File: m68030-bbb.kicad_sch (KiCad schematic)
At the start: 6 parts, among them U1 MC68030, U2 XC95108TQ100, U3 IS61C25616AL, U4 M29F400F, U5 IS61C25616AL, U6 M29F400F

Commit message: Add MPCC and PIT, move things around.  Still need to decide on CPLD to use.
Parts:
- removed U2: XC95108TQ100, Package_QFP:TQFP-100_14x14mm_P0.5mm, symbol CPLD_Xilinx:XC95108PQ100
- removed U3, U5: IS61C25616AL, Package_SO:TSOP-II-44_10.16x18.41mm_P0.8mm, symbol sbc-parts:IS61C25616AL
- removed U4, U6: M29F400F, Package_SO:TSOP-I-48_18.4x12mm_P0.5mm, symbol Memory_Flash:28F400
- added U10, U11, U8, U9: M29F160F, Package_SO:TSOP-I-48_18.4x12mm_P0.5mm, symbol sbc-parts:M29F160F
- added U2: R68561, Package_DIP:DIP-48_W15.24mm_Socket_LongPads, symbol retro-parts:R68561
- added U3: 68230, Package_DIP:DIP-48_W15.24mm_Socket_LongPads, symbol Interface:68230
- added U4, U5, U6, U7: CY62167GN-45ZXI, Package_SO:TSOP-I-48_18.4x12mm_P0.5mm, symbol sbc-parts:CY62167GN-45ZXI
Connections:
- net ~{BR}: now reaches U1.A1 (~{BR})
- net A17: now reaches U1.A10 (A17)
- net A17: now also U10.2 (A14), U11.2 (A14), U4.1 (A15), U5.1 (A15), U6.1 (A15), U7.1 (A15), U8.2 (A14), U9.2 (A14)
- net A15: now reaches U1.A11 (A15)
- net A15: now also U10.4 (A12), U11.4 (A12), U4.3 (A13), U5.3 (A13), U6.3 (A13), U7.3 (A13), U8.4 (A12), U9.4 (A12)
- net A13: now reaches U1.A12 (A13)
- net A13: now also U10.6 (A10), U11.6 (A10), U4.5 (A11), U5.5 (A11), U6.5 (A11), U7.5 (A11), U8.6 (A10), U9.6 (A10)
- net A10: now reaches U1.A13 (A10)
- net A10: now also U10.18 (A7), U11.18 (A7), U4.8 (A8), U5.8 (A8), U6.8 (A8), U7.8 (A8), U8.18 (A7), U9.18 (A7)
- net A0: now reaches U1.A2 (A0)
- net A30: now reaches U1.A3 (A30)
- net A28: now reaches U1.A4 (A28)
- net A26: now reaches U1.A5 (A26)
- net A24: now reaches U1.A6 (A24)
- net A23: now reaches U1.A7 (A23)
- net A21: now reaches U1.A8 (A21)
- net A21: now also U10.16 (A18), U11.16 (A18), U4.9 (A19), U5.9 (A19), U6.9 (A19), U7.9 (A19), U8.16 (A18), U9.16 (A18)
- net A19: now reaches U1.A9 (A19)
- net A19: now also U10.48 (A16), U11.48 (A16), U4.17 (A17), U5.17 (A17), U6.17 (A17), U7.17 (A17), U8.48 (A16), U9.48 (A16)
- net ~{RMC}: now reaches U1.B1 (~{RMC})
- net A14: now reaches U1.B10 (A14)
- net A14: now also U10.5 (A11), U11.5 (A11), U4.4 (A12), U5.4 (A12), U6.4 (A12), U7.4 (A12), U8.5 (A11), U9.5 (A11)
- net A12: now reaches U1.B11 (A12)
- net A12: now also U10.7 (A9), U11.7 (A9), U4.6 (A10), U5.6 (A10), U6.6 (A10), U7.6 (A10), U8.7 (A9), U9.7 (A9)
- net A8: now reaches U1.B12 (A8)
- net A8: now also U10.20 (A5), U11.20 (A5), U4.19 (A6), U5.19 (A6), U6.19 (A6), U7.19 (A6), U8.20 (A5), U9.20 (A5)
- net A7: now reaches U1.B13 (A7)
- net A7: now also U10.21 (A4), U11.21 (A4), U4.20 (A5), U5.20 (A5), U6.20 (A5), U7.20 (A5), U8.21 (A4), U9.21 (A4)
- net ~{BG}: now reaches U1.B2 (~{BG})
- net A31: now reaches U1.B3 (A31)
- net A29: now reaches U1.B4 (A29)
- net A27: now reaches U1.B5 (A27)
- net A25: now reaches U1.B6 (A25)
- net A22: now reaches U1.B7 (A22)
- net A22: now also U10.9 (A19), U11.9 (A19), U4.45 (DQ15/A20), U5.45 (DQ15/A20), U6.45 (DQ15/A20), U7.45 (DQ15/A20), U8.9 (A19), U9.9 (A19)
- net A20: now reaches U1.B8 (A20)
- net A20: now also U10.17 (A17), U11.17 (A17), U4.16 (A18), U5.16 (A18), U6.16 (A18), U7.16 (A18), U8.17 (A17), U9.17 (A17)
- net A16: now reaches U1.B9 (A16)
- net A16: now also U10.3 (A13), U11.3 (A13), U4.2 (A14), U5.2 (A14), U6.2 (A14), U7.2 (A14), U8.3 (A13), U9.3 (A13)
- net FC1: now reaches U1.C1 (FC1)
- net A11: now reaches U1.C10 (A11)
- net A11: now also U10.8 (A8), U11.8 (A8), U4.7 (A9), U5.7 (A9), U6.7 (A9), U7.7 (A9), U8.8 (A8), U9.8 (A8)
- net A9: now reaches U1.C11 (A9)
- net A9: now also U10.19 (A6), U11.19 (A6), U4.18 (A7), U5.18 (A7), U6.18 (A7), U7.18 (A7), U8.19 (A6), U9.19 (A6)
- net A5: now reaches U1.C12 (A5)
- net A5: now also U10.23 (A2), U11.23 (A2), U4.22 (A3), U5.22 (A3), U6.22 (A3), U7.22 (A3), U8.23 (A2), U9.23 (A2)
- net A4: now reaches U1.C13 (A4)
- net A4: now also U10.24 (A1), U11.24 (A1), U4.23 (A2), U5.23 (A2), U6.23 (A2), U7.23 (A2), U8.24 (A1), U9.24 (A1)
- net ~{BGACK}: now reaches U1.C3 (~{BGACK})
- net A1: now reaches U1.C4 (A1)
- net GND: now reaches U1.C5 (GND)
- net GND: now also U1.C7 (GND), U1.C9 (GND), U1.E11 (GND), U1.E3 (GND), U1.F3 (GND), U1.G11 (GND), U1.G3 (GND), U1.J11 (GND), U1.J3 (GND), U1.L5 (GND), U1.L7 (GND), U1.L8 (GND), U1.L9 (GND), U4.27 (VSS), U4.46 (VSS), U4.47 (~{BYTE}), U5.27 (VSS), U5.46 (VSS), U5.47 (~{BYTE}), U6.27 (VSS), U6.46 (VSS), U6.47 (~{BYTE}), U7.27 (VSS), U7.46 (VSS), U7.47 (~{BYTE})
- net +5V: now reaches U1.C6 (VCC)
- net +5V: now also U1.D10 (VCC), U1.D4 (VCC), U1.F11 (VCC), U1.F2 (VCC), U1.H11 (VCC), U1.H3 (VCC), U1.K10 (VCC), U1.K4 (VCC), U1.L6 (VCC)
- net A18: now reaches U1.C8 (A18)
- net A18: now also U10.1 (A15), U11.1 (A15), U4.48 (A16), U5.48 (A16), U6.48 (A16), U7.48 (A16), U8.1 (A15), U9.1 (A15)
- net FC2: now reaches U1.D1 (FC2)
- net A6: now reaches U1.D11 (A6)
- net A6: now also U10.22 (A3), U11.22 (A3), U4.21 (A4), U5.21 (A4), U6.21 (A4), U7.21 (A4), U8.22 (A3), U9.22 (A3)
- net A3: now reaches U1.D12 (A3)
- net A3: now also U10.25 (A0), U11.25 (A0), U4.24 (A1), U5.24 (A1), U6.24 (A1), U7.24 (A1), U8.25 (A0), U9.25 (A0)
- net A2: now reaches U1.D13 (A2)
- net A2: now also U4.25 (A0), U5.25 (A0), U6.25 (A0), U7.25 (A0), U8.45 (A-1/D15)
- net FC0: now reaches U1.D2 (FC0)
- net ~{OCS}: now reaches U1.D3 (~{OCS})
- net CLK: now reaches U1.E1 (CLK)
- net ~{IPEND}: now reaches U1.E13 (~{IPEND})
- net ~{AVEC}: now reaches U1.E2 (~{AVEC})
- net ~{DSACK0}: now reaches U1.F1 (~{DSACK0})
- net ~{RESET}: now reaches U1.F12 (~{RESET})
- net ~{STERM}: now reaches U1.G1 (~{STERM})
- net ~{IPL2}: now reaches U1.G12 (~{IPL2})
- net ~{IPL1}: now reaches U1.G13 (~{IPL1})
- net ~{DSACK1}: now reaches U1.G2 (~{DSACK1})
- net ~{BERR}: now reaches U1.H1 (~{BERR})
- net ~{IPL0}: now reaches U1.H13 (~{IPL0})
- net ~{HALT}: now reaches U1.H2 (~{HALT})
- net ~{AS}: now reaches U1.J2 (~{AS})
- net D5: now reaches U1.K11 (D5)
- net D5: now also U4.40 (DQ5), U8.40 (D5)
- net D1: now reaches U1.K12 (D1)
- net D1: now also U4.31 (DQ1), U8.31 (D1)
- net D0: now reaches U1.K13 (D0)
- net D0: now also U4.29 (DQ0), U8.29 (D0)
- net ~{DS}: now reaches U1.K2 (~{DS})
- net D10: now reaches U1.L10 (D10)
- net D10: now also U5.33 (DQ2), U9.33 (D2)
- net D7: now reaches U1.L11 (D7)
- net D7: now also U4.44 (DQ7), U8.44 (D7)
- net D4: now reaches U1.L12 (D4)
- net D4: now also U4.38 (DQ4), U8.38 (D4)
- net D2: now reaches U1.L13 (D2)
- net D2: now also U4.33 (DQ2), U8.33 (D2)
- net R/~{W}: now reaches U1.L3 (R/~{W})
- net D30: now reaches U1.L4 (D30)
- net D30: now also U11.42 (D6), U7.42 (DQ6)
- net D12: now reaches U1.M10 (D12)
- net D12: now also U5.38 (DQ4), U9.38 (D4)
- net D9: now reaches U1.M11 (D9)
- net D9: now also U5.31 (DQ1), U9.31 (D1)
- net D6: now reaches U1.M12 (D6)
- net D6: now also U4.42 (DQ6), U8.42 (D6)
- net D3: now reaches U1.M13 (D3)
- net D3: now also U4.35 (DQ3), U8.35 (D3)
- net ~{ECS}: now reaches U1.M2 (~{ECS})
- net D29: now reaches U1.M3 (D29)
- net D29: now also U11.40 (D5), U7.40 (DQ5)
- net D27: now reaches U1.M4 (D27)
- net D27: now also U11.35 (D3), U7.35 (DQ3)
- net D24: now reaches U1.M5 (D24)
- net D24: now also U11.29 (D0), U7.29 (DQ0)
- net D22: now reaches U1.M6 (D22)
- net D22: now also U10.42 (D6), U6.42 (DQ6)
- net D20: now reaches U1.M7 (D20)
- net D20: now also U10.38 (D4), U6.38 (DQ4)
- net D17: now reaches U1.M8 (D17)
- net D17: now also U10.31 (D1), U6.31 (DQ1)
- net D14: now reaches U1.M9 (D14)
- net D14: now also U5.42 (DQ6), U9.42 (D6)
- net D31: now reaches U1.N1 (D31)
- net D31: now also U11.44 (D7), U7.44 (DQ7)
- net D15: now reaches U1.N10 (D15)
- net D15: now also U5.44 (DQ7), U9.44 (D7)
- net D13: now reaches U1.N11 (D13)
- net D13: now also U5.40 (DQ5), U9.40 (D5)
- net D11: now reaches U1.N12 (D11)
- net D11: now also U5.35 (DQ3), U9.35 (D3)
- net D8: now reaches U1.N13 (D8)
- net D8: now also U5.29 (DQ0), U9.29 (D0)
- net D28: now reaches U1.N2 (D28)
- net D28: now also U11.38 (D4), U7.38 (DQ4)
- net D26: now reaches U1.N3 (D26)
- net D26: now also U11.33 (D2), U7.33 (DQ2)
- net D25: now reaches U1.N4 (D25)
- net D25: now also U11.31 (D1), U7.31 (DQ1)
- net D23: now reaches U1.N5 (D23)
- net D23: now also U10.44 (D7), U6.44 (DQ7)
- net D21: now reaches U1.N6 (D21)
- net D21: now also U10.40 (D5), U6.40 (DQ5)
- net D19: now reaches U1.N7 (D19)
- net D19: now also U10.35 (D3), U6.35 (DQ3)
- net D18: now reaches U1.N8 (D18)
- net D18: now also U10.33 (D2), U6.33 (DQ2)
- net D16: now reaches U1.N9 (D16)
- net D16: now also U10.29 (D0), U6.29 (DQ0)
- new net: U5.12 (CE2), U5.14 (UB#), U5.15 (LB#)
- new net: U7.12 (CE2), U7.14 (UB#), U7.15 (LB#)
- new net: U4.12 (CE2), U4.14 (UB#), U4.15 (LB#)
- new net: U6.12 (CE2), U6.14 (UB#), U6.15 (LB#)
- new net ~{RAMCE}: U4.26 (CE#), U5.26 (CE#), U6.26 (CE#), U7.26 (CE#)
- new net ~{RDLL}: U10.26 (~{CE}), U11.26 (~{CE}), U4.28 (OE#), U8.26 (~{CE}), U9.26 (~{CE})
- new net ~{RDLM}: U5.28 (OE#)
- new net ~{RDUM}: U6.28 (OE#)
- new net ~{RDUU}: U7.28 (OE#)
- new net ~{ROMCE}: U10.28 (~{OE}), U11.28 (~{OE}), U8.28 (~{OE}), U9.28 (~{OE})
- new net ~{WELL}: U10.11 (~{WE}), U11.11 (~{WE}), U4.11 (WE#), U8.11 (~{WE}), U9.11 (~{WE})
- new net ~{WELM}: U5.11 (WE#)
- new net ~{WEUM}: U6.11 (WE#)
- new net ~{WEUU}: U7.11 (WE#)
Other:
- moved on the sheet: U1

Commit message: More CPLD changes
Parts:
- added U12: XC95108TQ100, Package_QFP:TQFP-100_14x14mm_P0.5mm, symbol retro-parts:XC95108TQ100
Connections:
- net +5V: now also U12.26 (VCCIO), U12.38 (VCCIO), U12.5 (VCCINT), U12.51 (VCCIO), U12.57 (VCCINT), U12.88 (VCCIO), U12.98 (VCCINT)
- net FC0: now also U12.9 (FB2_M14)
- net FC1: now also U12.10 (FB2_M15)
- net FC2: now also U12.11 (FB2_M16)
- net GND: now also U12.100 (GND), U12.21 (GND), U12.31 (GND), U12.44 (GND), U12.62 (GND), U12.69 (GND), U12.75 (GND), U12.84 (GND)
- net R/~{W}: now also U12.17 (FB1_M8)
- net ~{AS}: now also U12.15 (FB1_M5)
- net ~{DSACK0}: now also U12.6 (FB2_M11)
- net ~{DSACK1}: now also U12.7 (FB2_M10)
- net ~{DS}: now also U12.16 (FB1_M6)
- net ~{ECS}: now also U12.13 (FB1_M2)
- net ~{OCS}: now also U12.14 (FB1_M3)
- net ~{RMC}: now also U12.19 (FB1_M4)
- net ~{STERM}: now also U12.8 (FB2_M12)
- net ~{CIOUT}: now reaches U1.C2 (~{CIOUT})
- net ~{CBACK}: now reaches U1.J1 (~{CBACK})
- net ~{CBREQ}: now reaches U1.K1 (~{CBREQ})
- net ~{SIZ1}: now reaches U1.K3 (SIZ1)
- net ~{SIZ1}: now also U12.20 (FB1_M11)
- net ~{CIIN}: now reaches U1.L1 (~{CIIN})
- net ~{SIZ0}: now reaches U1.L2 (SIZ0)
- net ~{SIZ0}: now also U12.24 (FB1_M10)
- net CLK renamed CPUCLK
- net CPUCLK: now also U12.22 (FB1_M12_GCLK1)
- new net SYSCLK: U12.23 (FB1_M14_GCLK2)
- new net SYSCLK2X: U12.27 (FB1_M16_GCLK3)
- new net ~{SYSRESET}: U12.99 (FB2_M5_GSR)
- no-connect marks 0 -> 1

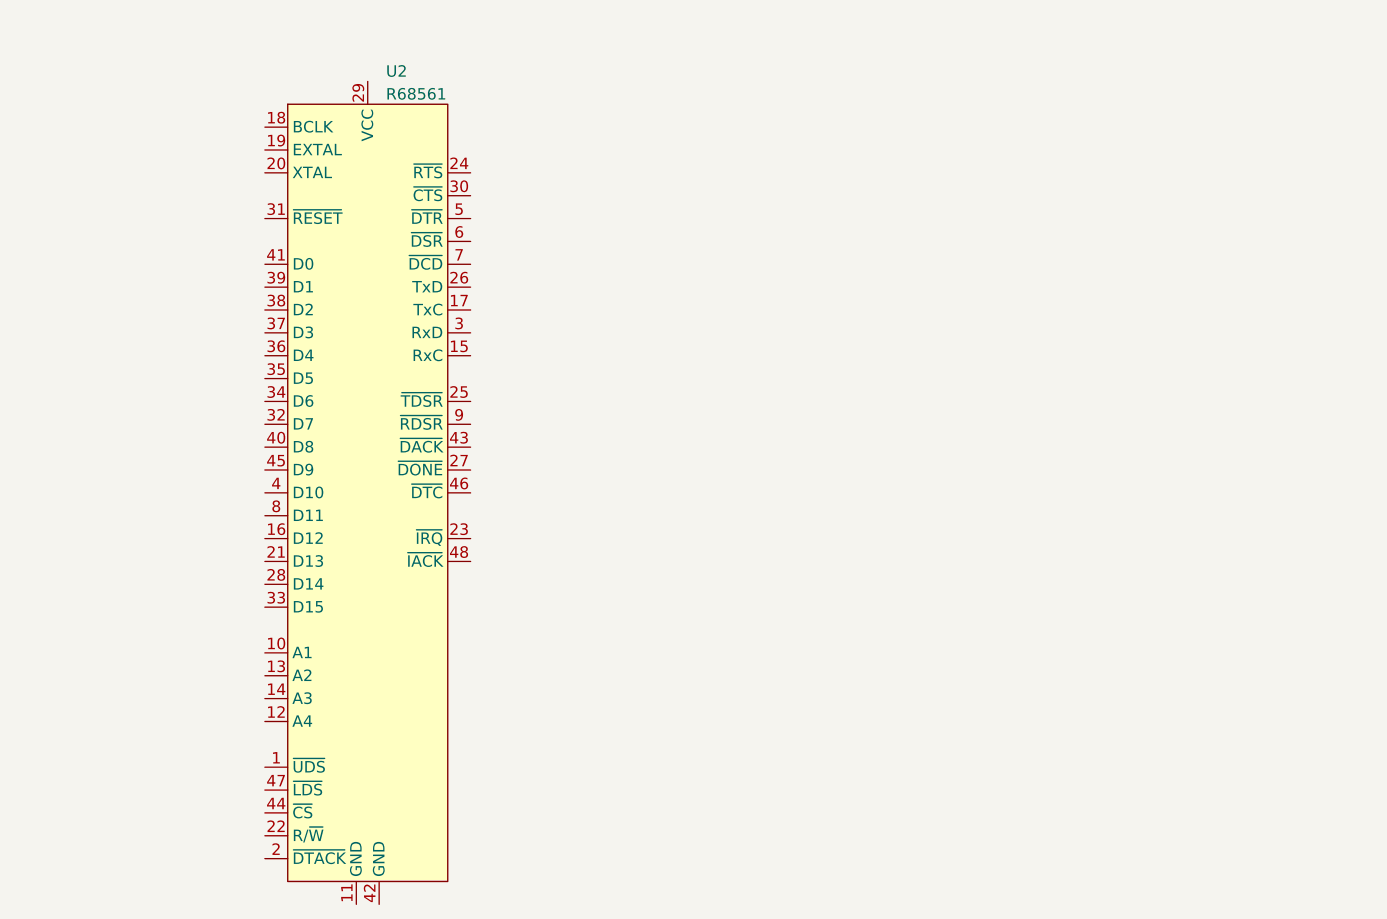
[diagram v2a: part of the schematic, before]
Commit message: More CPLD changes, counter and comparitor for DTACK generation testing in sim.
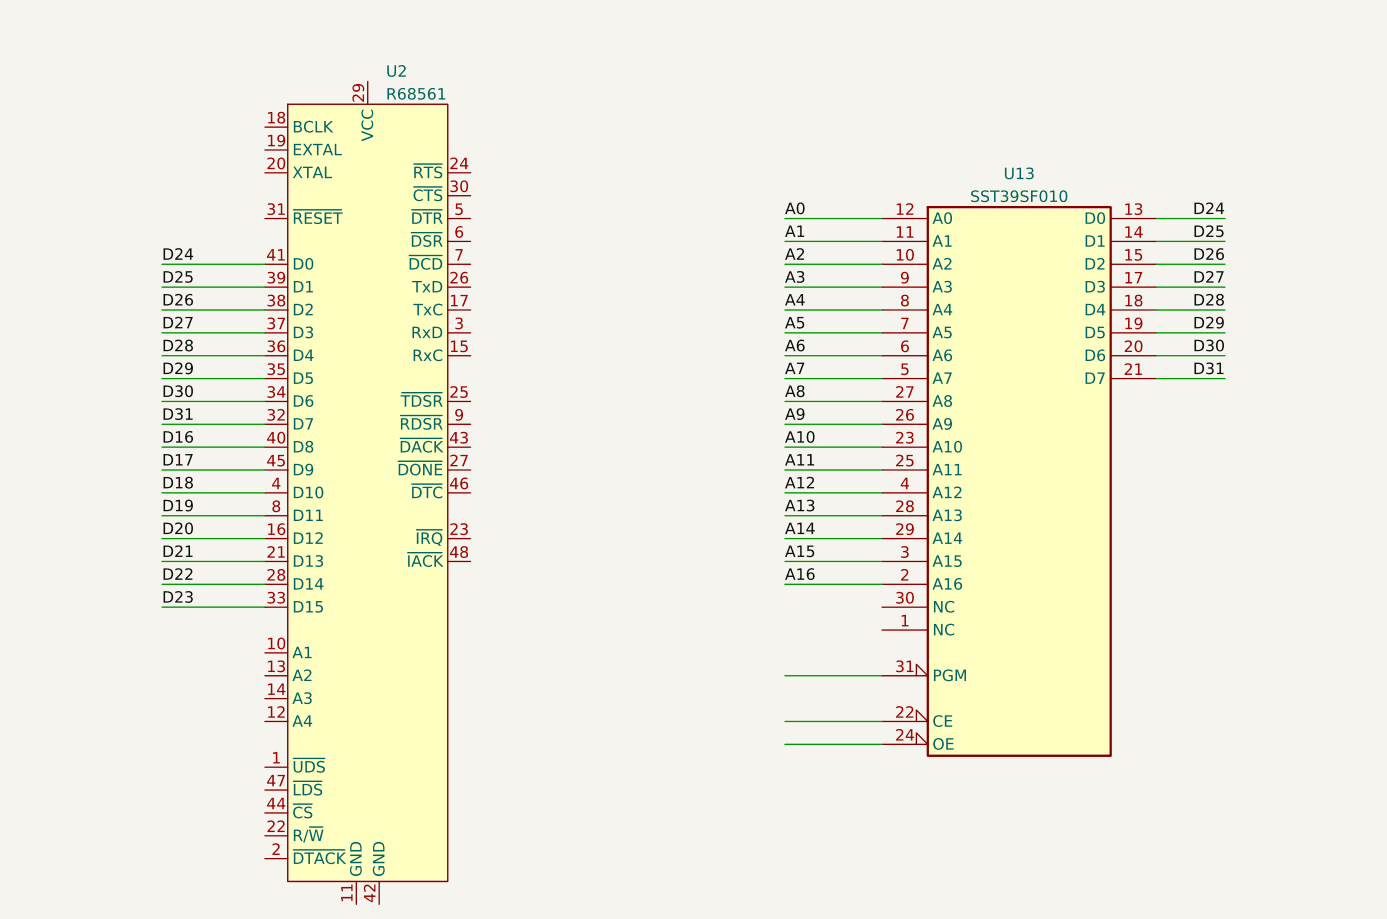
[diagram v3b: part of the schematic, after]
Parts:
- added U13: SST39SF010, Package_DIP:DIP-32_W15.24mm_Socket_LongPads, symbol Memory_Flash:SST39SF010
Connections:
- net A0: now also U13.12 (A0)
- net A1: now also U13.11 (A1)
- net A10: now also U13.23 (A10)
- net A11: now also U13.25 (A11)
- net A12: now also U13.4 (A12)
- net A13: now also U13.28 (A13)
- net A14: now also U13.29 (A14)
- net A15: now also U13.3 (A15)
- net A16: now also U13.2 (A16)
- net A2: now also U13.10 (A2)
- net A3: now also U13.9 (A3)
- net A4: now also U13.8 (A4)
- net A5: now also U13.7 (A5)
- net A6: now also U13.6 (A6)
- net A7: now also U13.5 (A7)
- net A8: now also U13.27 (A8)
- net A9: now also U13.26 (A9)
- net D16: now also U2.40 (D8)
- net D17: now also U2.45 (D9)
- net D18: now also U2.4 (D10)
- net D19: now also U2.8 (D11)
- net D20: now also U2.16 (D12)
- net D21: now also U2.21 (D13)
- net D22: now also U2.28 (D14)
- net D23: now also U2.33 (D15)
- net D24: now also U2.41 (D0), U13.13 (D0)
- net D25: now also U2.39 (D1), U13.14 (D1)
- net D26: now also U2.38 (D2), U13.15 (D2)
- net D27: now also U2.37 (D3), U13.17 (D3)
- net D28: now also U2.36 (D4), U13.18 (D4)
- net D29: now also U2.35 (D5), U13.19 (D5)
- net D30: now also U2.34 (D6), U13.20 (D6)
- net D31: now also U2.32 (D7), U13.21 (D7)
- net GND: now also U13.16 (GND)
- new net VCC: U13.32 (VCC)

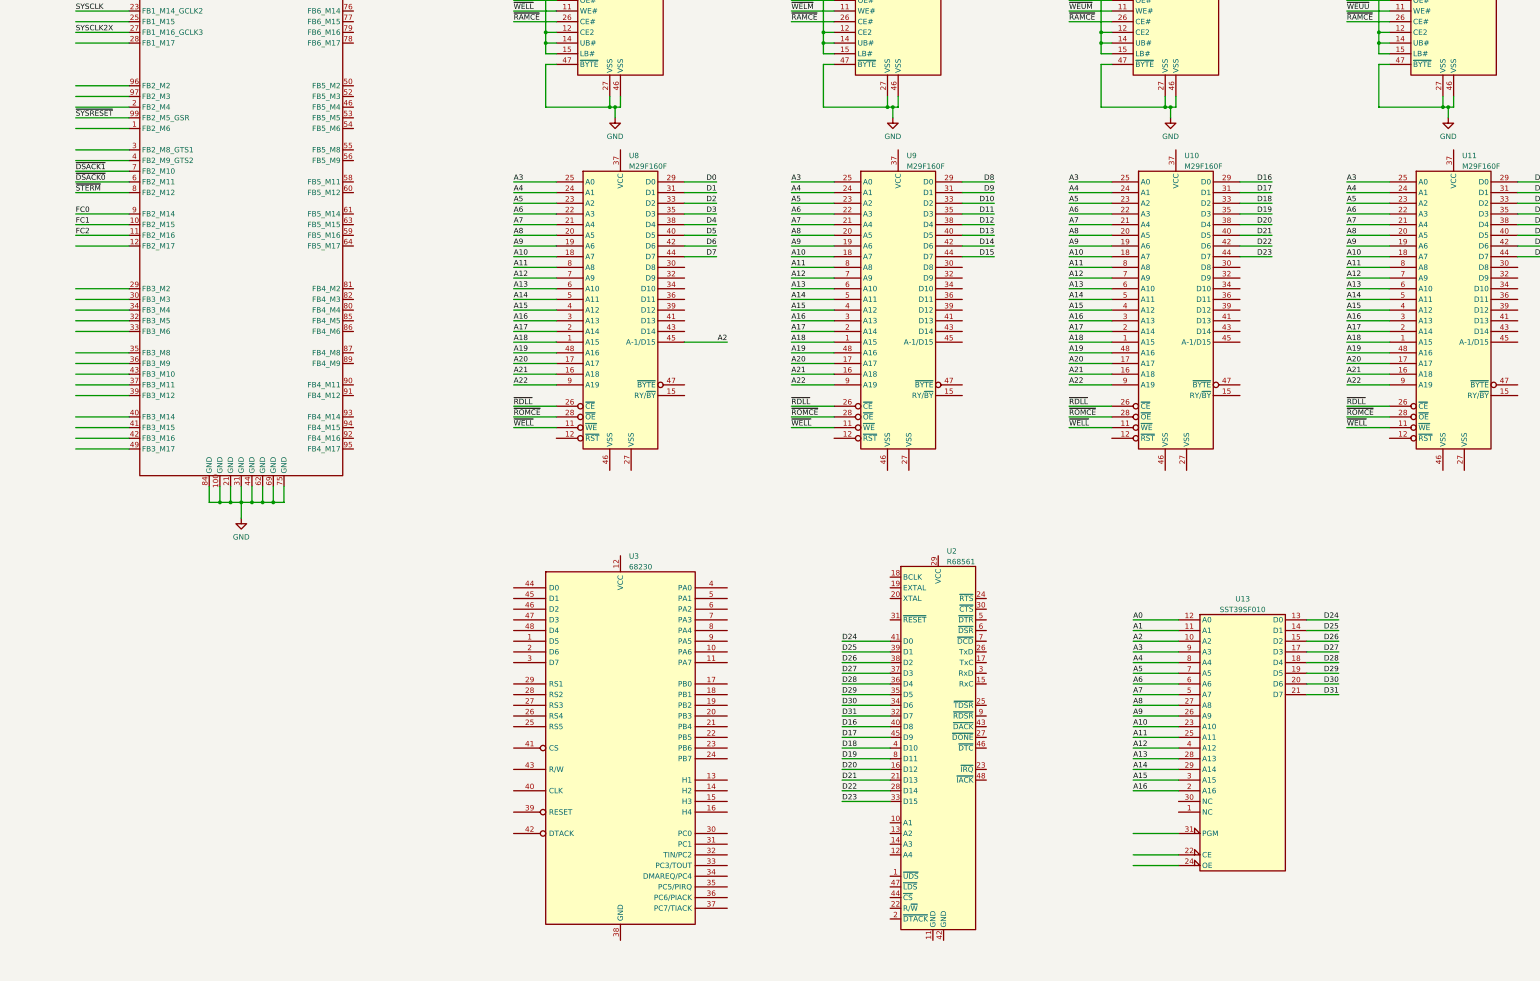
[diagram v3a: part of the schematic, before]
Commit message: Filled the CPLD... Not 100% sure this will run at 25MHz...  Maybe 20 or 16, design could probably use some optimization.
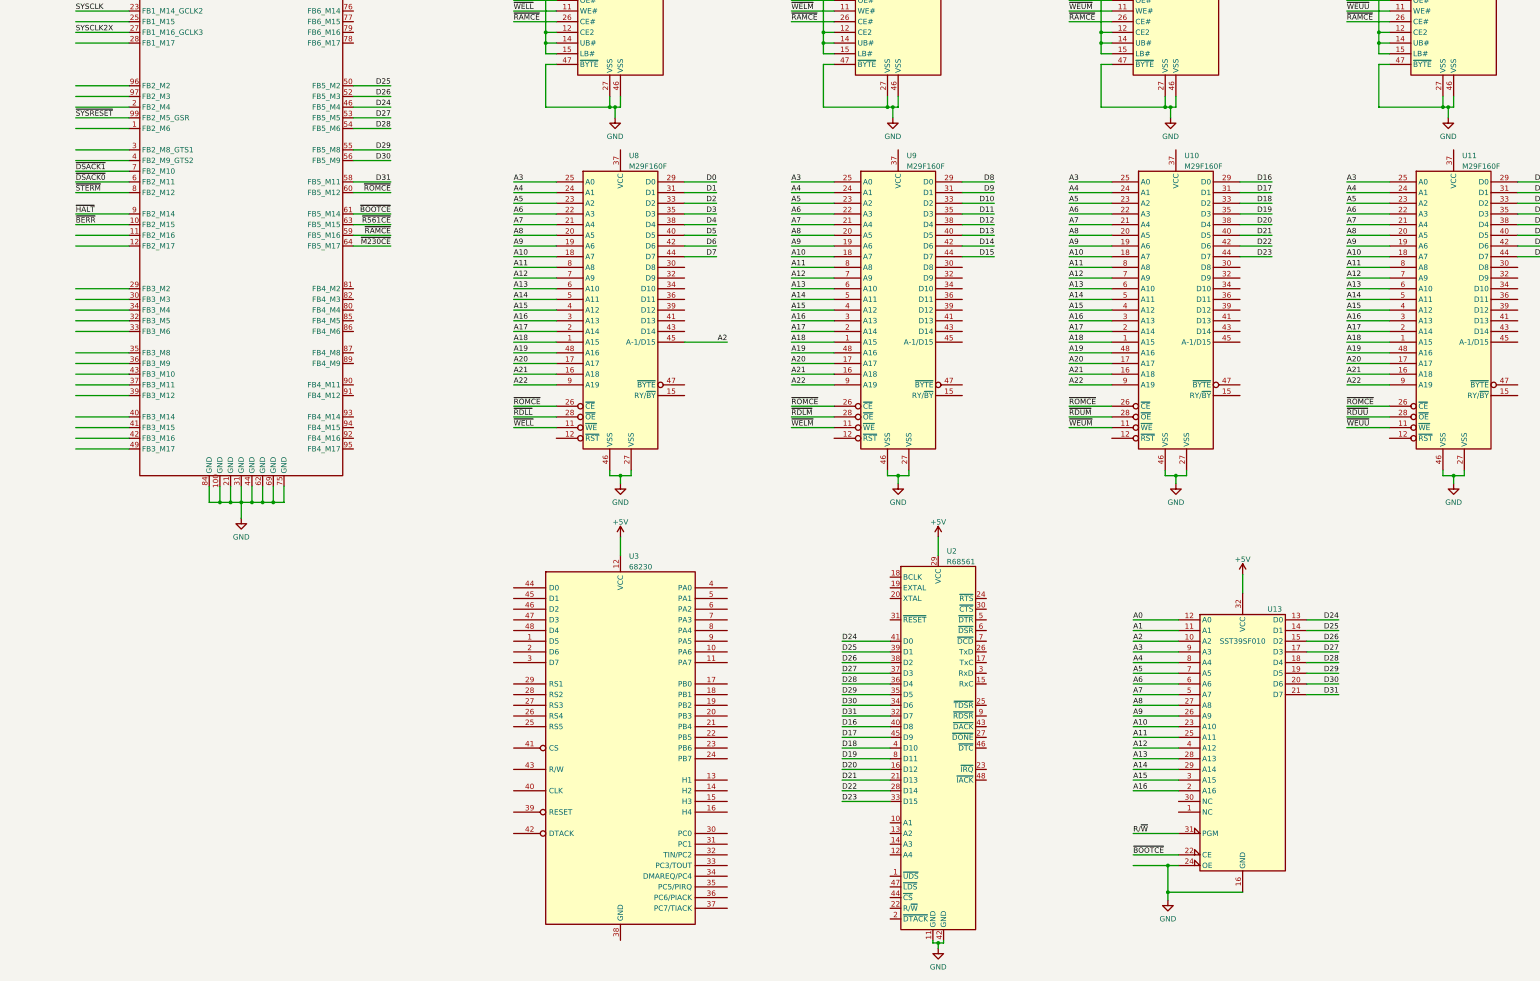
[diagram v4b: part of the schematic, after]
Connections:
- net VCC is gone; now on net +5V: U13.32 (VCC)
- net +5V: now also U2.29 (VCC), U3.12 (VCC)
- net D24: now also U12.46 (FB5_M4)
- net D25: now also U12.50 (FB5_M2)
- net D26: now also U12.52 (FB5_M3)
- net D27: now also U12.53 (FB5_M5)
- net D28: now also U12.54 (FB5_M6)
- net D29: now also U12.55 (FB5_M8)
- net D30: now also U12.56 (FB5_M9)
- net D31: now also U12.58 (FB5_M11)
- net FC0: no longer U12.9 (FB2_M14)
- net FC1: no longer U12.10 (FB2_M15)
- net FC2: no longer U12.11 (FB2_M16)
- net GND: now also U10.27 (VSS), U10.46 (VSS), U11.27 (VSS), U11.46 (VSS), U13.24 (OE), U2.11 (GND), U2.42 (GND), U8.27 (VSS), U8.46 (VSS), U9.27 (VSS), U9.46 (VSS)
- net R/~{W}: now also U13.31 (PGM)
- net ~{BERR}: now also U12.10 (FB2_M15)
- net ~{HALT}: now also U12.9 (FB2_M14)
- net ~{RAMCE}: now also U12.59 (FB5_M16)
- net ~{RDLL}: now also U8.28 (~{OE}); no longer U10.26 (~{CE}), U11.26 (~{CE}), U8.26 (~{CE}), U9.26 (~{CE})
- net ~{RDLM}: now also U9.28 (~{OE})
- net ~{RDUM}: now also U10.28 (~{OE})
- net ~{RDUU}: now also U11.28 (~{OE})
- net ~{ROMCE}: now also U10.26 (~{CE}), U11.26 (~{CE}), U12.60 (FB5_M12), U8.26 (~{CE}), U9.26 (~{CE}); no longer U10.28 (~{OE}), U11.28 (~{OE}), U8.28 (~{OE}), U9.28 (~{OE})
- net ~{WELL}: no longer U10.11 (~{WE}), U11.11 (~{WE}), U9.11 (~{WE})
- net ~{WELM}: now also U9.11 (~{WE})
- net ~{WEUM}: now also U10.11 (~{WE})
- net ~{WEUU}: now also U11.11 (~{WE})
- net ~{BOOTCE}: now reaches U12.61 (FB5_M14)
- net ~{BOOTCE}: now also U13.22 (CE)
- net ~{R561CE}: now reaches U12.63 (FB5_M15)
- net ~{M230CE}: now reaches U12.64 (FB5_M17)
